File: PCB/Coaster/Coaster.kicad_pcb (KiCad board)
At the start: 2 copper layers, 198 x 98 mm, 138 parts, among them J1 USB-C, J2 Shelly, J3 Join, P1 TestPoint, P10 TestPoint, P11 TestPoint, P12 TestPoint, P2 TestPoint, P3 TestPoint, P4 TestPoint, P5 TestPoint, P6 TestPoint, P7 TestPoint, P8 TestPoint, P9 TestPoint, T1 TestPoint, T10 TestPoint, T11 TestPoint, T12 TestPoint, T2 TestPoint, T3 TestPoint, T4 TestPoint, T5 TestPoint, T6 TestPoint, T7 TestPoint, T8 TestPoint, T9 TestPoint, U1 ESP32-PICO-MINI-02, U2 LMR16006XDDCR, U3 QR

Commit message: Grr
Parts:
- moved P12 1.00 mm to (114.0, 85.0)
- moved P3 1.00 mm to (114.0, 88.0)
- moved P4 1.00 mm to (114.0, 91.0)
- moved P5 1.00 mm to (114.0, 82.0)
- moved P6 1.00 mm to (114.0, 94.0)
- moved T12 1.00 mm to (186.0, 85.0)
- moved T3 1.00 mm to (186.0, 88.0)
- moved T4 1.00 mm to (186.0, 91.0)
- moved T5 1.00 mm to (186.0, 82.0)
- moved T6 1.00 mm to (186.0, 94.0)
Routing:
- net GPIO0: track 17.9 -> 0.00 mm
- net +3V3: track 61.4 -> 78.9 mm
- net O: track 11.5 -> 0.00 mm
- net +3.3VA: track 9.12 -> 0.00 mm
- net I: track 3.46 -> 0.00 mm
- net Net-(P6-Pad1): track 10.4 -> 11.4 mm
- net Net-(P4-Pad1): track 8.16 -> 9.16 mm
- net Net-(P3-Pad1): track 7.49 -> 8.35 mm
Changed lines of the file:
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@@
     (property "Sheetname" "")
     (attr smd)
-    (fp_text reference "C49" (at 0 -1.43 90) (layer "F.SilkS")
+    (fp_text reference "C49" (at 0 -1.43 90) (layer "F.SilkS") hide
       (effects (font (size 1 1) (thickness 0.15)))
     )
@@
   )
   (footprint "RevK:PAD-LINK" (layer "F.Cu")
-    (at 187 91)
+    (at 186 91)
     (property "Sheetfile" "Coaster.kicad_sch")
     (property "Sheetname" "")
@@
   )
   (footprint "RevK:PAD-LINK" (layer "F.Cu")
-    (at 187 85)
+    (at 186 85)
     (property "Sheetfile" "Coaster.kicad_sch")
     (property "Sheetname" "")
@@
   )
   (footprint "RevK:PAD-LINK" (layer "F.Cu")
-    (at 187 88)
+    (at 186 88)
     (property "Sheetfile" "Coaster.kicad_sch")
     (property "Sheetname" "")
@@
   )
   (footprint "RevK:PAD" (layer "F.Cu")
-    (at 113 91)
+    (at 114 91)
     (property "Sheetfile" "Coaster.kicad_sch")
     (property "Sheetname" "")
@@
   )
   (footprint "RevK:PAD" (layer "F.Cu")
-    (at 113 82)
+    (at 114 82)
     (property "Sheetfile" "Coaster.kicad_sch")
     (property "Sheetname" "")
@@
   )
   (footprint "RevK:PAD-LINK" (layer "F.Cu")
-    (at 187 94)
+    (at 186 94)
     (property "Sheetfile" "Coaster.kicad_sch")
     (property "Sheetname" "")
@@
   )
   (footprint "RevK:PAD" (layer "F.Cu")
-    (at 113 85)
+    (at 114 85)
     (property "Sheetfile" "Coaster.kicad_sch")
     (property "Sheetname" "")
@@
   )
   (footprint "RevK:PAD" (layer "F.Cu")
-    (at 113 88)
+    (at 114 88)
     (property "Sheetfile" "Coaster.kicad_sch")
     (property "Sheetname" "")
@@
   )
   (footprint "RevK:PAD-LINK" (layer "F.Cu")
-    (at 187 82)
+    (at 186 82)
     (property "Sheetfile" "Coaster.kicad_sch")
     (property "Sheetname" "")
@@
   )
   (footprint "RevK:PAD" (layer "F.Cu")
-    (at 113 94)
+    (at 114 94)
     (property "Sheetfile" "Coaster.kicad_sch")
     (property "Sheetname" "")
@@
   (segment (start 186 138) (end 198.35 138) (width 0.25) (layer "F.Cu") (net 3))
   (arc (start 198.35 138) (mid 199.87028 137.37028) (end 200.5 135.85) (width 0.25) (layer "F.Cu") (net 3))
-  (segment (start 92 87.175) (end 92 78) (width 0.25) (layer "F.Cu") (net 4))
-  (segment (start 113 78) (end 113 82) (width 0.25) (layer "F.Cu") (net 4))
+  (segment (start 86 75) (end 86 84) (width 0.25) (layer "F.Cu") (net 4))
+  (segment (start 114 82) (end 114 75) (width 0.25) (layer "F.Cu") (net 4))
   (segment (start 94.1 86.6) (end 92.575 86.6) (width 0.25) (layer "F.Cu") (net 4))
   (segment (start 98.203828 96.353828) (end 93.821172 96.353828) (width 0.25) (layer "F.Cu") (net 4))
-  (segment (start 94 76) (end 111 76) (width 0.25) (layer "F.Cu") (net 4))
+  (segment (start 112 73) (end 88 73) (width 0.25) (layer "F.Cu") (net 4))
   (segment (start 91 88.175) (end 91 95.175) (width 0.25) (layer "F.Cu") (net 4))
+  (segment (start 89 87) (end 91.825 87) (width 0.25) (layer "F.Cu") (net 4))
   (arc (start 93.821172 96.353828) (mid 93.240516 96.594344) (end 93 97.175) (width 0.25) (layer "F.Cu") (net 4))
   (arc (start 91 95.175) (mid 91.585786 96.589214) (end 93 97.175) (width 0.25) (layer "F.Cu") (net 4))
+  (arc (start 114 75) (mid 113.414214 73.585786) (end 112 73) (width 0.25) (layer "F.Cu") (net 4))
   (arc (start 92 87.175) (mid 91.292893 87.467893) (end 91 88.175) (width 0.25) (layer "F.Cu") (net 4))
-  (arc (start 92 78) (mid 92.585786 76.585786) (end 94 76) (width 0.25) (layer "F.Cu") (net 4))
   (arc (start 92.575 86.6) (mid 92.168414 86.768414) (end 92 87.175) (width 0.25) (layer "F.Cu") (net 4))
-  (arc (start 111 76) (mid 112.414214 76.585786) (end 113 78) (width 0.25) (layer "F.Cu") (net 4))
+  (arc (start 91.825 87) (mid 91.948744 87.051256) (end 92 87.175) (width 0.25) (layer "F.Cu") (net 4))
+  (arc (start 86 84) (mid 86.87868 86.12132) (end 89 87) (width 0.25) (layer "F.Cu") (net 4))
+  (arc (start 88 73) (mid 86.585786 73.585786) (end 86 75) (width 0.25) (layer "F.Cu") (net 4))
   (arc (start 101.8 99.95) (mid 100.746706 97.407122) (end 98.203828 96.353828) (width 0.25) (layer "F.Cu") (net 4))
-  (segment (start 183 86.46) (end 182.04 86.46) (width 0.25) (layer "F.Cu") (net 5))
-  (segment (start 185 96) (end 182.5 96) (width 0.25) (layer "F.Cu") (net 5))
-  (segment (start 180.5 94) (end 180.5 88) (width 0.25) (layer "F.Cu") (net 5))
-  (arc (start 182.5 96) (mid 181.085786 95.414214) (end 180.5 94) (width 0.25) (layer "F.Cu") (net 5))
-  (arc (start 182.04 86.46) (mid 180.951056 86.911056) (end 180.5 88) (width 0.25) (layer "F.Cu") (net 5))
-  (arc (start 187 94) (mid 186.414214 95.414214) (end 185 96) (width 0.25) (layer "F.Cu") (net 5))
-  (segment (start 183 91.54) (end 186.46 91.54) (width 0.25) (layer "F.Cu") (net 6))
-  (segment (start 189 90) (end 189 90.5) (width 0.25) (layer "F.Cu") (net 7))
-  (segment (start 187 92.5) (end 184.58 92.5) (width 0.25) (layer "F.Cu") (net 7))
-  (arc (start 184.58 92.5) (mid 183.462771 92.962771) (end 183 94.08) (width 0.25) (layer "F.Cu") (net 7))
-  (arc (start 189 90.5) (mid 188.414214 91.914214) (end 187 92.5) (width 0.25) (layer "F.Cu") (net 7))
-  (arc (start 187 88) (mid 188.414214 88.585786) (end 189 90) (width 0.25) (layer "F.Cu") (net 7))
   (segment (start 207 140) (end 207 139.065) (width 1) (layer "F.Cu") (net 34))
   (segment (start 193 140) (end 207 140) (width 1) (layer "F.Cu") (net 34))
@@
   (segment (start 165.48 109.68) (end 166.3 109.46) (width 0.25) (layer "F.Cu") (net 39))
   (segment (start 166.53 110.24) (end 166.78 111.03) (width 0.25) (layer "F.Cu") (net 39))
-  (segment (start 185 87) (end 185 84) (width 0.25) (layer "F.Cu") (net 40))
-  (arc (start 185 84) (mid 185.585786 82.585786) (end 187 82) (width 0.25) (layer "F.Cu") (net 40))
-  (arc (start 183 89) (mid 184.414214 88.414214) (end 185 87) (width 0.25) (layer "F.Cu") (net 40))
   (segment (start 172.2 121.26) (end 172.7 121.91) (width 0.25) (layer "F.Cu") (net 41))
   (segment (start 170.32 118.56) (end 170.77 119.25) (width 0.25) (layer "F.Cu") (net 41))
@@
   (segment (start 199.58 64.15) (end 199.59 65) (width 0.25) (layer "F.Cu") (net 68))
   (segment (start 197.12 65.12) (end 196.31 65.2) (width 0.25) (layer "F.Cu") (net 68))
-  (segment (start 106.5 88.2) (end 105.9 88.2) (width 0.25) (layer "F.Cu") (net 69))
-  (segment (start 106.8 88.5) (end 106.5 88.2) (width 0.25) (layer "F.Cu") (net 69))
-  (segment (start 112.5 88.5) (end 107.3 88.5) (width 0.25) (layer "F.Cu") (net 69))
-  (segment (start 107.3 88.5) (end 106.8 88.5) (width 0.25) (layer "F.Cu") (net 69))
-  (arc (start 113 88) (mid 112.853553 88.353553) (end 112.5 88.5) (width 0.25) (layer "F.Cu") (net 69))
-  (segment (start 105.9 89) (end 111 89) (width 0.25) (layer "F.Cu") (net 70))
-  (arc (start 111 89) (mid 112.414214 89.585786) (end 113 91) (width 0.25) (layer "F.Cu") (net 70))
+  (segment (start 106.8 88.5) (end 112.792894 88.5) (width 0.25) (layer "F.Cu") (net 69))
+  (segment (start 105.9 88.2) (end 106.5 88.2) (width 0.25) (layer "F.Cu") (net 69))
+  (segment (start 106.5 88.2) (end 106.8 88.5) (width 0.25) (layer "F.Cu") (net 69))
+  (arc (start 112.792894 88.5) (mid 113.446175 88.370054) (end 114 88) (width 0.25) (layer "F.Cu") (net 69))
+  (segment (start 105.9 89) (end 112 89) (width 0.25) (layer "F.Cu") (net 70))
+  (arc (start 112 89) (mid 113.414214 89.585786) (end 114 91) (width 0.25) (layer "F.Cu") (net 70))
+  (segment (start 113 95) (end 112 95) (width 0.25) (layer "F.Cu") (net 71))
   (segment (start 104.45 95) (end 112 95) (width 0.25) (layer "F.Cu") (net 71))
   (segment (start 104 93.9) (end 104 94.55) (width 0.25) (layer "F.Cu") (net 71))
   (arc (start 104 94.55) (mid 104.131802 94.868198) (end 104.45 95) (width 0.25) (layer "F.Cu") (net 71))
-  (arc (start 112 95) (mid 112.707107 94.707107) (end 113 94) (width 0.25) (layer "F.Cu") (net 71))
+  (arc (start 113 95) (mid 113.707107 94.707107) (end 114 94) (width 0.25) (layer "F.Cu") (net 71))
   (segment (start 113 128) (end 113 137) (width 0.25) (layer "F.Cu") (net 72))
   (segment (start 119 91) (end 119 122) (width 0.25) (layer "F.Cu") (net 72))
@@
   (arc (start 119 122) (mid 117.828427 124.828427) (end 115 126) (width 0.25) (layer "F.Cu") (net 72))
   (arc (start 115 126) (mid 113.585786 126.585786) (end 113 128) (width 0.25) (layer "F.Cu") (net 72))
+  (zone (net 0) (net_name "") (layers F&B.Cu) (hatch edge 0.508)
+    (connect_pads (clearance 0))
+    (min_thickness 0.254)
+    (keepout (tracks not_allowed) (vias not_allowed) (pads not_allowed) (copperpour not_allowed) (footprints allowed))
+    (fill (thermal_gap 0.508) (thermal_bridge_width 0.508))
+    (polygon
+      (pts
+        (xy 112 83.4)
+        (xy 88 83.4)
+        (xy 88 75)
+        (xy 112 75)
+      )
+    )
+  )
   (zone (net 35) (net_name "GND2") (layer "F.Cu") (hatch edge 0.508)
     (connect_pads (clearance 0.2))
@@
     (polygon
       (pts
-        (xy 213 83.4)
-        (xy 189 83.4)
-        (xy 189 75)
-        (xy 213 75)
+        (xy 212 83.4)
+        (xy 188 83.4)
+        (xy 188 75)
+        (xy 212 75)
       )
     )

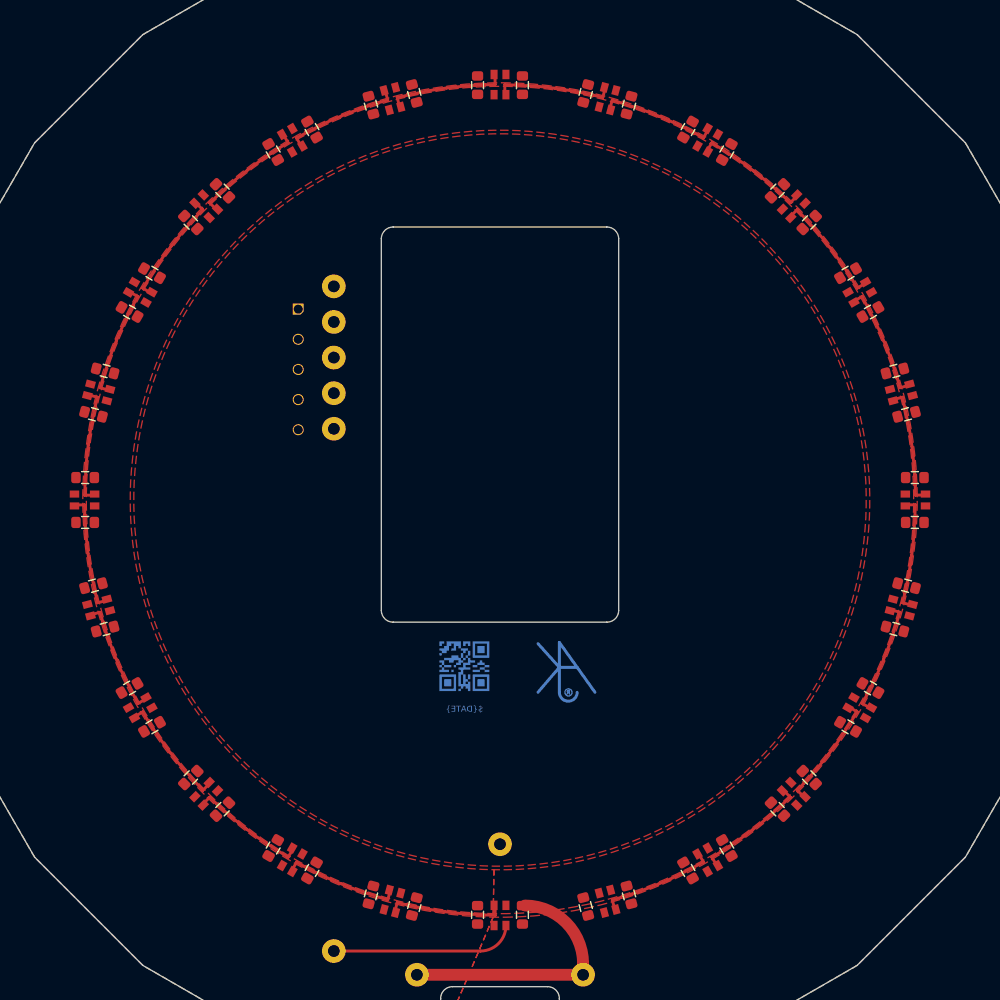
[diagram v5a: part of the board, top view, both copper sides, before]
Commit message: Fix stupid position error
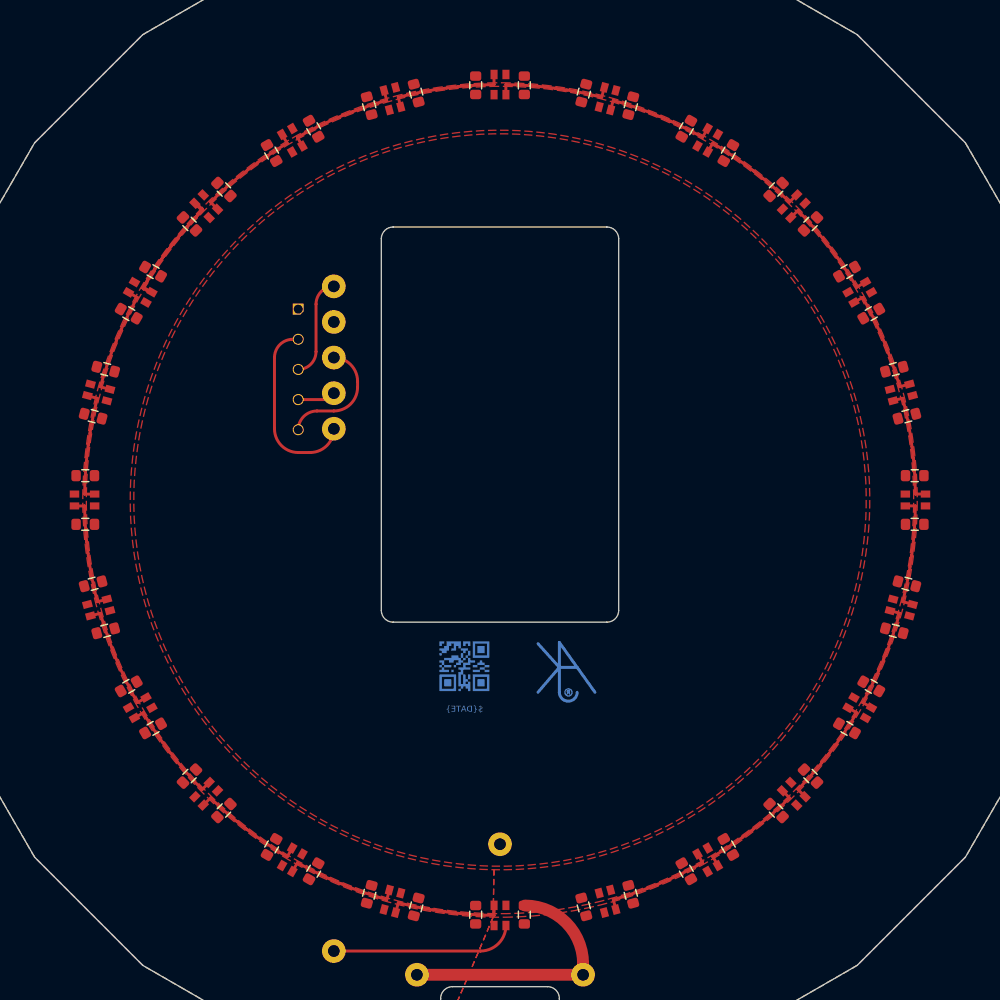
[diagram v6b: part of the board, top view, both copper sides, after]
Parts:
- moved C16 0.16 mm to (223.3, 73.8)
- moved C34 0.16 mm to (176.7, 73.8)
- moved C4 0.16 mm to (176.7, 126.2)
- moved C46 0.16 mm to (223.3, 126.2)
- moved C14 0.16 mm to (207.1, 65.7)
- moved C2 0.16 mm to (192.9, 134.3)
- moved C20 0.16 mm to (234.3, 107.1)
- moved C30 0.16 mm to (165.7, 107.1)
- moved C36 0.16 mm to (192.9, 65.7)
- moved C42 0.16 mm to (234.3, 92.9)
- moved C48 0.16 mm to (207.1, 134.3)
- moved C8 0.16 mm to (165.7, 92.9)
- moved C10 0.16 mm to (173.8, 76.7)
- moved C22 0.16 mm to (226.2, 123.3)
- moved C28 0.16 mm to (173.8, 123.3)
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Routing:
- net GPIO0: track 0.00 -> 15.9 mm
- net O: track 0.00 -> 10.5 mm
- net Net-(D10-Pad4): track 10.0 -> 19.9 mm
- net +3.3VA: track 0.00 -> 8.59 mm
- net I: track 0.00 -> 3.29 mm

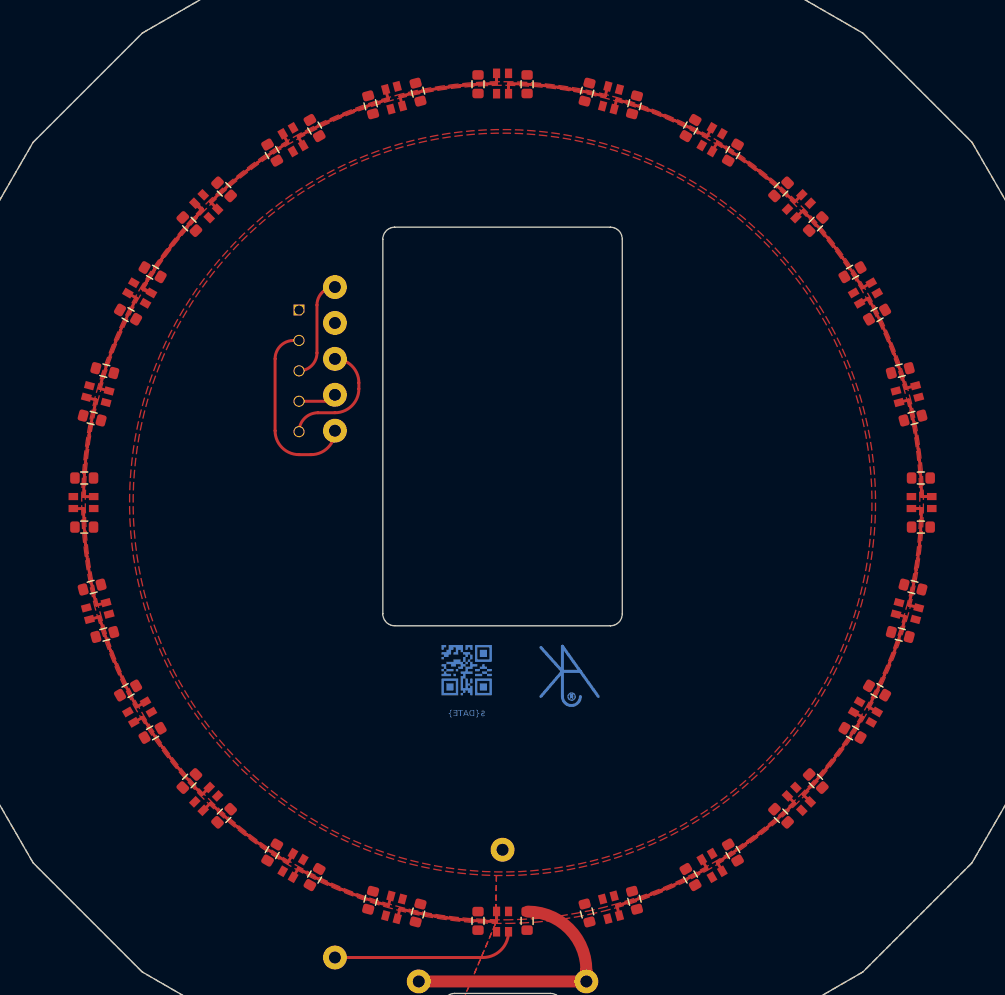
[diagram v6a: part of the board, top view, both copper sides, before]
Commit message: Better curvey tracks for this
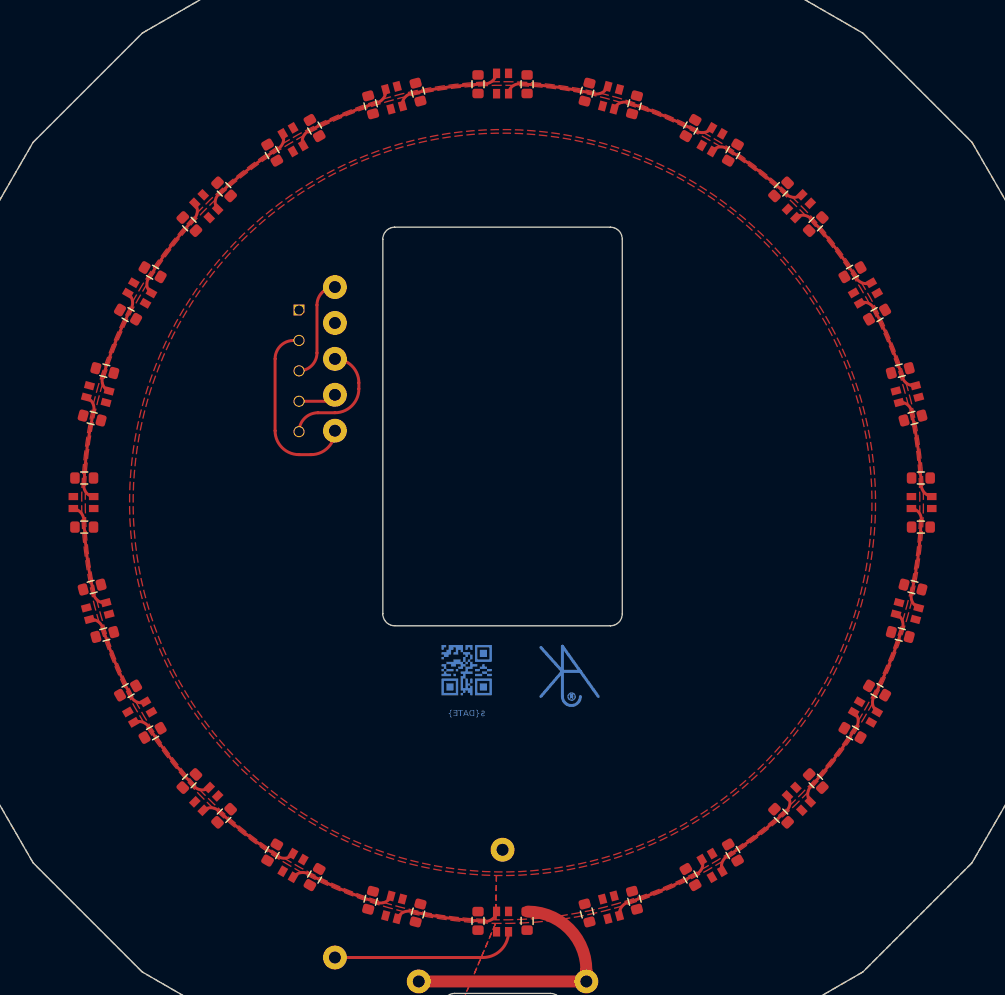
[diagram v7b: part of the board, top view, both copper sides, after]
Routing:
- net Net-(D10-Pad4): track 19.9 -> 8.99 mm
- net Net-(D23-Pad2): track 9.87 -> 8.98 mm
- net Net-(D11-Pad2): track 9.87 -> 8.98 mm
- net Net-(D5-Pad2): track 9.87 -> 8.98 mm
- net Net-(D17-Pad2): track 9.87 -> 8.98 mm
- net Net-(D21-Pad2): track 9.87 -> 8.99 mm
- net Net-(D15-Pad2): track 9.87 -> 8.99 mm
- net Net-(D3-Pad2): track 9.87 -> 8.99 mm
- net Net-(D13-Pad2): track 9.87 -> 8.99 mm
- net Net-(D7-Pad2): track 9.87 -> 8.99 mm
- net Net-(D19-Pad2): track 9.87 -> 8.99 mm
- net Net-(D1-Pad2): track 9.87 -> 8.99 mm
- net Net-(D16-Pad2): track 9.86 -> 8.99 mm
- net Net-(D4-Pad2): track 9.86 -> 8.99 mm
- net Net-(D22-Pad2): track 9.86 -> 8.99 mm
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
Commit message: Further tidy
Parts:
- moved U3 4.00 mm to (193.0, 114.0)
- moved Logo1 1.75 mm to (206.8, 114.1)
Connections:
- U1 pad 33: GND -> unconnected-(U1-Pad33)
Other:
- board text added: "${DATE}"
